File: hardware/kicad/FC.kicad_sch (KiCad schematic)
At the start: 6 parts, among them J6 xt30, U9 TPS7A4533DCQR

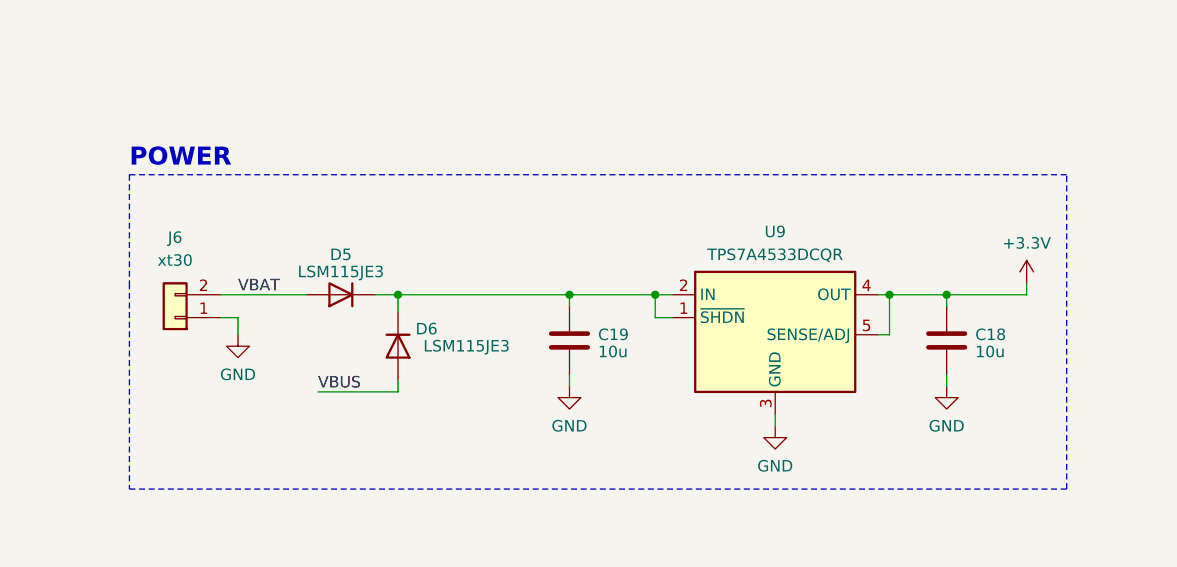
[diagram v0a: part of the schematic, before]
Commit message: assigned footprints
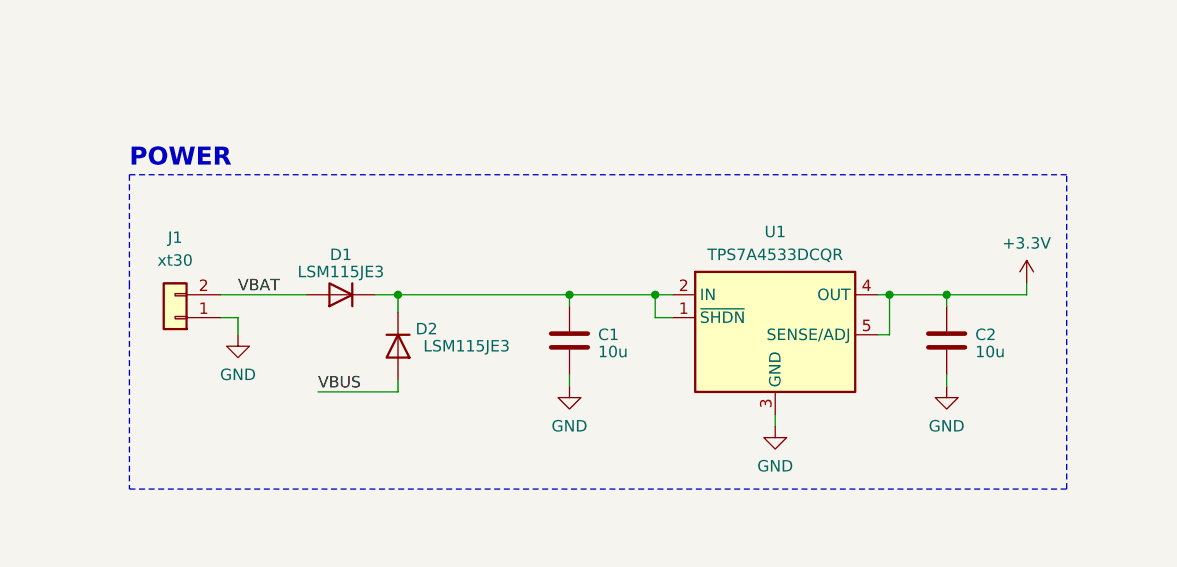
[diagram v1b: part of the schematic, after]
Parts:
- C1: renamed from C19; footprint (none) -> Resistor_SMD:R_0603_1608Metric
- C2: renamed from C18; footprint (none) -> Resistor_SMD:R_0603_1608Metric
- renumbered D5 to D1, D6 to D2, J6 to J1, U9 to U1
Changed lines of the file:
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@@
   (symbol (lib_id "Device:C") (at 208.915 152.4 0) (unit 1)
     (in_bom yes) (on_board yes) (dnp no)
-    (property "Reference" "C19" (at 212.09 151.765 0)
+    (property "Reference" "C1" (at 212.09 151.765 0)
       (effects (font (size 1.27 1.27)) (justify left))
     )
@@
       (effects (font (size 1.27 1.27)) (justify left))
     )
-    (property "Footprint" "" (at 209.8802 156.21 0)
+    (property "Footprint" "Resistor_SMD:R_0603_1608Metric" (at 209.8802 156.21 0)
       (effects (font (size 1.27 1.27)) hide)
     )
@@
       (project "FC"
         (path "/54cce219-8b98-4e71-96c4-f9ee784aa3bc"
-          (reference "C19") (unit 1)
+          (reference "C1") (unit 1)
         )
       )
@@
   (symbol (lib_id "Regulator_Linear:TPS7A05285PDBV") (at 231.775 149.86 0) (unit 1)
     (in_bom yes) (on_board yes) (dnp no) (fields_autoplaced)
-    (property "Reference" "U9" (at 231.775 140.335 0)
+    (property "Reference" "U1" (at 231.775 140.335 0)
       (effects (font (size 1.27 1.27)))
     )
@@
       (project "FC"
         (path "/54cce219-8b98-4e71-96c4-f9ee784aa3bc"
-          (reference "U9") (unit 1)
+          (reference "U1") (unit 1)
         )
       )
@@
   (symbol (lib_id "power:GND") (at 172.085 151.765 0) (unit 1)
     (in_bom yes) (on_board yes) (dnp no) (fields_autoplaced)
-    (property "Reference" "#PWR047" (at 172.085 158.115 0)
+    (property "Reference" "#PWR01" (at 172.085 158.115 0)
       (effects (font (size 1.27 1.27)) hide)
     )
@@
       (project "FC"
         (path "/54cce219-8b98-4e71-96c4-f9ee784aa3bc"
-          (reference "#PWR047") (unit 1)
+          (reference "#PWR01") (unit 1)
         )
       )
@@
   (symbol (lib_id "power:+3.3V") (at 259.715 146.05 0) (unit 1)
     (in_bom yes) (on_board yes) (dnp no) (fields_autoplaced)
-    (property "Reference" "#PWR045" (at 259.715 149.86 0)
+    (property "Reference" "#PWR05" (at 259.715 149.86 0)
       (effects (font (size 1.27 1.27)) hide)
     )
@@
       (project "FC"
         (path "/54cce219-8b98-4e71-96c4-f9ee784aa3bc"
-          (reference "#PWR045") (unit 1)
+          (reference "#PWR05") (unit 1)
         )
       )
@@
   (symbol (lib_id "Connector_Generic:Conn_01x02") (at 165.1 149.86 180) (unit 1)
     (in_bom yes) (on_board yes) (dnp no) (fields_autoplaced)
-    (property "Reference" "J6" (at 165.1 140.97 0)
+    (property "Reference" "J1" (at 165.1 140.97 0)
       (effects (font (size 1.27 1.27)))
     )
@@
       (project "FC"
         (path "/54cce219-8b98-4e71-96c4-f9ee784aa3bc"
-          (reference "J6") (unit 1)
+          (reference "J1") (unit 1)
         )
       )
@@
   (symbol (lib_id "power:GND") (at 250.825 157.48 0) (unit 1)
     (in_bom yes) (on_board yes) (dnp no) (fields_autoplaced)
-    (property "Reference" "#PWR043" (at 250.825 163.83 0)
+    (property "Reference" "#PWR04" (at 250.825 163.83 0)
       (effects (font (size 1.27 1.27)) hide)
     )
@@
       (project "FC"
         (path "/54cce219-8b98-4e71-96c4-f9ee784aa3bc"
-          (reference "#PWR043") (unit 1)
+          (reference "#PWR04") (unit 1)
         )
       )
@@
   (symbol (lib_id "Device:D") (at 183.515 147.32 180) (unit 1)
     (in_bom yes) (on_board yes) (dnp no)
-    (property "Reference" "D5" (at 183.515 142.875 0)
+    (property "Reference" "D1" (at 183.515 142.875 0)
       (effects (font (size 1.27 1.27)))
     )
@@
       (project "FC"
         (path "/54cce219-8b98-4e71-96c4-f9ee784aa3bc"
-          (reference "D5") (unit 1)
+          (reference "D1") (unit 1)
         )
       )
@@
   (symbol (lib_id "Device:C") (at 250.825 152.4 0) (unit 1)
     (in_bom yes) (on_board yes) (dnp no)
-    (property "Reference" "C18" (at 254 151.765 0)
+    (property "Reference" "C2" (at 254 151.765 0)
       (effects (font (size 1.27 1.27)) (justify left))
     )
@@
       (effects (font (size 1.27 1.27)) (justify left))
     )
-    (property "Footprint" "" (at 251.7902 156.21 0)
+    (property "Footprint" "Resistor_SMD:R_0603_1608Metric" (at 251.7902 156.21 0)
       (effects (font (size 1.27 1.27)) hide)
     )
@@
       (project "FC"
         (path "/54cce219-8b98-4e71-96c4-f9ee784aa3bc"
-          (reference "C18") (unit 1)
+          (reference "C2") (unit 1)
         )
       )
@@
   (symbol (lib_id "power:GND") (at 231.775 161.925 0) (unit 1)
     (in_bom yes) (on_board yes) (dnp no) (fields_autoplaced)
-    (property "Reference" "#PWR046" (at 231.775 168.275 0)
+    (property "Reference" "#PWR03" (at 231.775 168.275 0)
       (effects (font (size 1.27 1.27)) hide)
     )
@@
       (project "FC"
         (path "/54cce219-8b98-4e71-96c4-f9ee784aa3bc"
-          (reference "#PWR046") (unit 1)
+          (reference "#PWR03") (unit 1)
         )
       )
@@
   (symbol (lib_id "power:GND") (at 208.915 157.48 0) (unit 1)
     (in_bom yes) (on_board yes) (dnp no) (fields_autoplaced)
-    (property "Reference" "#PWR044" (at 208.915 163.83 0)
+    (property "Reference" "#PWR02" (at 208.915 163.83 0)
       (effects (font (size 1.27 1.27)) hide)
     )
@@
       (project "FC"
         (path "/54cce219-8b98-4e71-96c4-f9ee784aa3bc"
-          (reference "#PWR044") (unit 1)
+          (reference "#PWR02") (unit 1)
         )
       )
@@
   (symbol (lib_id "Device:D") (at 189.865 153.035 270) (unit 1)
     (in_bom yes) (on_board yes) (dnp no)
-    (property "Reference" "D6" (at 193.04 151.13 90)
+    (property "Reference" "D2" (at 193.04 151.13 90)
       (effects (font (size 1.27 1.27)))
     )
@@
       (project "FC"
         (path "/54cce219-8b98-4e71-96c4-f9ee784aa3bc"
-          (reference "D6") (unit 1)
-        )
-      )
+          (reference "D2") (unit 1)
+        )
+      )

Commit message: all footprints have been fixed
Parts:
- D1, D2: footprint (none) -> LSM115JE3:LSM115JE3
- J1: footprint (none) -> XT30PW-M:AMASS_XT30PW-M; Amazon (none) -> https://www.amazon.com/Amass-XT30PW-Upgrade-Connectors-Batt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
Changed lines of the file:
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@@
       (effects (font (size 1.27 1.27)))
     )
-    (property "Footprint" "" (at 165.1 149.86 0)
+    (property "Footprint" "XT30PW-M:AMASS_XT30PW-M" (at 162.56 139.7 0)
       (effects (font (size 1.27 1.27)) hide)
     )
     (property "Datasheet" "~" (at 165.1 149.86 0)
+      (effects (font (size 1.27 1.27)) hide)
+    )
+    (property "Amazon" "https://www.amazon.com/Amass-XT30PW-Upgrade-Connectors-Battery/dp/B099F2PXYN#customerReviews" (at 162.56 139.7 0)
       (effects (font (size 1.27 1.27)) hide)
     )
@@
       (effects (font (size 1.27 1.27)))
     )
-    (property "Footprint" "" (at 183.515 147.32 0)
+    (property "Footprint" "LSM115JE3:LSM115JE3" (at 183.515 147.32 0)
       (effects (font (size 1.27 1.27)) hide)
     )
@@
       (effects (font (size 1.27 1.27)))
     )
-    (property "Footprint" "" (at 189.865 153.035 0)
+    (property "Footprint" "LSM115JE3:LSM115JE3" (at 189.865 153.035 0)
       (effects (font (size 1.27 1.27)) hide)
     )

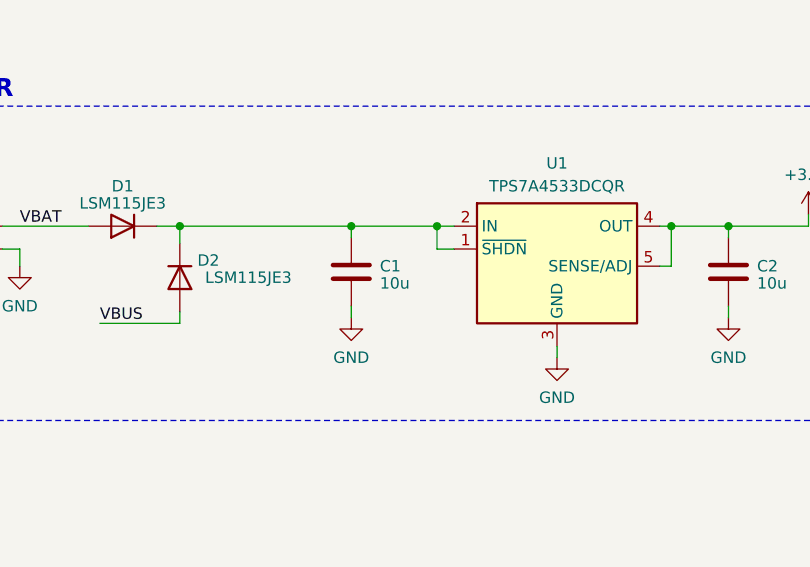
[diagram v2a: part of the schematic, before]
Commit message: changed cap footprint
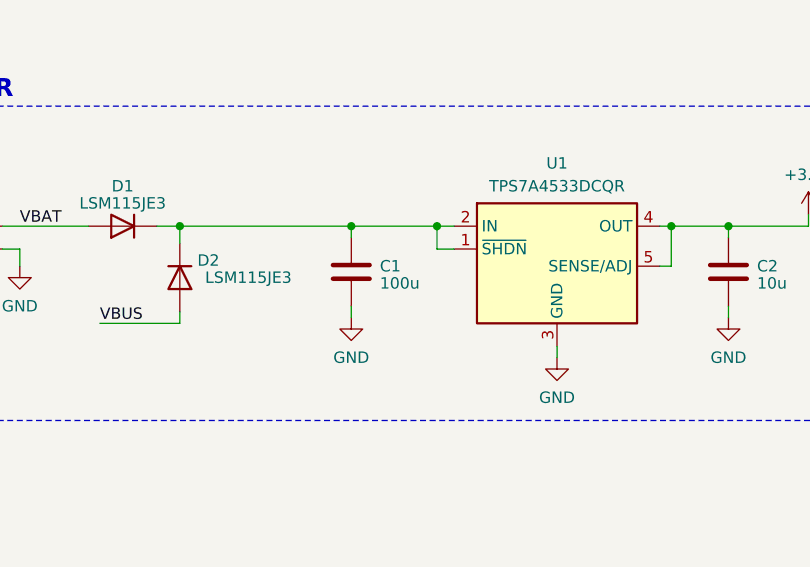
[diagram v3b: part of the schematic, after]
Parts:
- C1: value 10u -> 100u; footprint Resistor_SMD:R_0603_1608Metric -> Resistor_SMD:R_1206_3216Metric
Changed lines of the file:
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@@
       (effects (font (size 1.27 1.27)) (justify left))
     )
-    (property "Value" "10u" (at 212.09 153.67 0)
+    (property "Value" "100u" (at 212.09 153.67 0)
       (effects (font (size 1.27 1.27)) (justify left))
     )
-    (property "Footprint" "Resistor_SMD:R_0603_1608Metric" (at 209.8802 156.21 0)
+    (property "Footprint" "Resistor_SMD:R_1206_3216Metric" (at 209.8802 156.21 0)
       (effects (font (size 1.27 1.27)) hide)
     )

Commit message: ready for pcb
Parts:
- added D8: V15PM153, Package_TO_SOT_SMD:TO-277A, symbol Device:D_Schottky
- added F4: 30A, Resistor_SMD:R_1206_3216Metric, symbol Device:Fuse
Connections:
- net GND: now also D8.1 (A), D8.2 (A)
- net VBAT: now also D8.3 (K), F4.2; no longer J1.2 (N)
- new net: F4.1, J1.2 (N)
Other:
- moved on the sheet: J1
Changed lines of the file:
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@@
     (company "Missouri S&T Rocket Design Team")
   )
+  (junction (at 153.67 147.32) (diameter 0) (color 0 0 0 0)
+  )
   (junction (at 80.01 52.07) (diameter 0) (color 0 0 0 0)
+  )
+  (junction (at 153.67 156.21) (diameter 0) (color 0 0 0 0)
   )
   (junction (at 244.475 147.32) (diameter 0) (color 0 0 0 0)
@@
     (stroke (width 0) (type default))
   )
-  (wire (pts (xy 172.085 149.86) (xy 172.085 151.765))
-    (stroke (width 0) (type default))
-  )
   (wire (pts (xy 82.55 39.37) (xy 90.17 39.37))
     (stroke (width 0) (type default))
@@
     (stroke (width 0) (type default))
   )
+  (wire (pts (xy 134.62 147.32) (xy 142.24 147.32))
+    (stroke (width 0) (type default))
+  )
   (bus (pts (xy 154.94 52.07) (xy 192.405 52.07))
     (stroke (width 0) (type default))
@@
   )
   (wire (pts (xy 59.69 116.205) (xy 69.85 116.205))
+    (stroke (width 0) (type default))
+  )
+  (wire (pts (xy 136.525 156.21) (xy 153.67 156.21))
     (stroke (width 0) (type default))
   )
@@
     (stroke (width 0) (type default))
   )
-  (polyline (pts (xy 160.02 146.05) (xy 160.02 168.91))
-    (stroke (width 0) (type dash))
-  )
   (bus (pts (xy 15.24 180.34) (xy 15.24 184.15))
     (stroke (width 0) (type default))
   )
-  (wire (pts (xy 170.18 149.86) (xy 172.085 149.86))
+  (wire (pts (xy 153.67 156.21) (xy 153.67 158.115))
     (stroke (width 0) (type default))
   )
@@
     (stroke (width 0) (type dash))
   )
+  (wire (pts (xy 153.67 155.575) (xy 153.67 156.21))
+    (stroke (width 0) (type default))
+  )
   (wire (pts (xy 187.325 147.32) (xy 189.865 147.32))
     (stroke (width 0) (type default))
@@
     (stroke (width 0) (type dash))
   )
+  (wire (pts (xy 153.67 147.32) (xy 179.705 147.32))
+    (stroke (width 0) (type default))
+  )
   (bus (pts (xy 69.85 41.91) (xy 69.85 45.085))
     (stroke (width 0) (type default))
@@
   )
   (bus (pts (xy 229.87 41.91) (xy 229.87 45.085))
+    (stroke (width 0) (type default))
+  )
+  (wire (pts (xy 134.62 149.86) (xy 136.525 149.86))
     (stroke (width 0) (type default))
   )
@@
     (stroke (width 0) (type default))
   )
-  (polyline (pts (xy 160.02 133.985) (xy 160.02 146.05))
-    (stroke (width 0) (type dash))
-  )
   (wire (pts (xy 17.78 170.18) (xy 31.115 170.18))
     (stroke (width 0) (type default))
@@
     (stroke (width 0) (type default))
   )
+  (wire (pts (xy 153.67 147.32) (xy 153.67 147.955))
+    (stroke (width 0) (type default))
+  )
   (wire (pts (xy 59.69 123.825) (xy 69.85 123.825))
     (stroke (width 0) (type default))
@@
     (stroke (width 0) (type default))
   )
-  (wire (pts (xy 170.18 147.32) (xy 179.705 147.32))
+  (wire (pts (xy 149.86 147.32) (xy 153.67 147.32))
+    (stroke (width 0) (type default))
+  )
+  (wire (pts (xy 136.525 149.86) (xy 136.525 156.21))
     (stroke (width 0) (type default))
   )
@@
     )
   )
-  (symbol (lib_id "power:GND") (at 172.085 151.765 0) (unit 1)
+  (symbol (lib_id "power:GND") (at 153.67 158.115 0) (unit 1)
     (in_bom yes) (on_board yes) (dnp no) (fields_autoplaced)
-    (property "Reference" "#PWR01" (at 172.085 158.115 0)
-      (effects (font (size 1.27 1.27)) hide)
-    )
-    (property "Value" "GND" (at 172.085 156.21 0)
-      (effects (font (size 1.27 1.27)))
-    )
-    (property "Footprint" "" (at 172.085 151.765 0)
-      (effects (font (size 1.27 1.27)) hide)
-    )
-    (property "Datasheet" "" (at 172.085 151.765 0)
+    (property "Reference" "#PWR01" (at 153.67 164.465 0)
+      (effects (font (size 1.27 1.27)) hide)
+    )
+    (property "Value" "GND" (at 153.67 162.56 0)
+      (effects (font (size 1.27 1.27)))
+    )
+    (property "Footprint" "" (at 153.67 158.115 0)
+      (effects (font (size 1.27 1.27)) hide)
+    )
+    (property "Datasheet" "" (at 153.67 158.115 0)
       (effects (font (size 1.27 1.27)) hide)
     )
@@
     )
   )
-  (symbol (lib_id "Connector_Generic:Conn_01x02") (at 165.1 149.86 180) (unit 1)
+  (symbol (lib_id "Connector_Generic:Conn_01x02") (at 129.54 149.86 180) (unit 1)
     (in_bom yes) (on_board yes) (dnp no) (fields_autoplaced)
-    (property "Reference" "J1" (at 165.1 140.97 0)
-      (effects (font (size 1.27 1.27)))
-    )
-    (property "Value" "xt30" (at 165.1 143.51 0)
-      (effects (font (size 1.27 1.27)))
-    )
-    (property "Footprint" "XT30PW-M:AMASS_XT30PW-M" (at 162.56 139.7 0)
-      (effects (font (size 1.27 1.27)) hide)
-    )
-    (property "Datasheet" "~" (at 165.1 149.86 0)
-      (effects (font (size 1.27 1.27)) hide)
-    )
-    (property "Amazon" "https://www.amazon.com/Amass-XT30PW-Upgrade-Connectors-Battery/dp/B099F2PXYN#customerReviews" (at 162.56 139.7 0)
+    (property "Reference" "J1" (at 129.54 140.97 0)
+      (effects (font (size 1.27 1.27)))
+    )
+    (property "Value" "xt30" (at 129.54 143.51 0)
+      (effects (font (size 1.27 1.27)))
+    )
+    (property "Footprint" "XT30PW-M:AMASS_XT30PW-M" (at 127 139.7 0)
+      (effects (font (size 1.27 1.27)) hide)
+    )
+    (property "Datasheet" "~" (at 129.54 149.86 0)
+      (effects (font (size 1.27 1.27)) hide)
+    )
+    (property "Amazon" "https://www.amazon.com/Amass-XT30PW-Upgrade-Connectors-Battery/dp/B099F2PXYN#customerReviews" (at 127 139.7 0)
       (effects (font (size 1.27 1.27)) hide)
     )
@@
     )
   )
+  (symbol (lib_id "Device:D_Schottky") (at 153.67 151.765 270) (unit 1)
+    (in_bom yes) (on_board yes) (dnp no) (fields_autoplaced)
+    (property "Reference" "D8" (at 156.21 150.8125 90)
+      (effects (font (size 1.27 1.27)) (justify left))
+    )
+    (property "Value" "V15PM153" (at 156.21 153.3525 90)
+      (effects (font (size 1.27 1.27)) (justify left))
+    )
+    (property "Footprint" "Package_TO_SOT_SMD:TO-277A" (at 163.83 154.305 0)
+      (effects (font (size 1.27 1.27)) hide)
+    )
+    (property "Datasheet" "https://www.vishay.com/docs/87206/v15pm153.pdf" (at 163.83 154.305 0)
+      (effects (font (size 1.27 1.27)) hide)
+    )
+    (property "Digikey" "https://www.digikey.com/en/products/detail/vishay-general-semiconductor-diodes-division/V15PM153-M3-I/16683129" (at 163.83 154.305 0)
+      (effects (font (size 1.27 1.27)) hide)
+    )
+    (pin "3")
+    (pin "2")
+    (pin "1")
+    (instances
+      (project "FC"
+        (path "/54cce219-8b98-4e71-96c4-f9ee784aa3bc"
+          (reference "D8") (unit 1)
+        )
+      )
+    )
+  )
   (symbol (lib_id "Device:D") (at 183.515 147.32 180) (unit 1)
     (in_bom yes) (on_board yes) (dnp no)
@@
         )
       )
+    )
+  )
+  (symbol (lib_id "Device:Fuse") (at 146.05 147.32 90) (unit 1)
+    (in_bom yes) (on_board yes) (dnp no)
+    (property "Reference" "F4" (at 146.05 143.51 90)
+      (effects (font (size 1.27 1.27)))
+    )
+    (property "Value" "30A" (at 146.05 145.415 90)
+      (effects (font (size 1.27 1.27)))
+    )
+    (property "Footprint" "Resistor_SMD:R_1206_3216Metric" (at 146.05 149.098 90)
+      (effects (font (size 1.27 1.27)) hide)
+    )
+    (property "Datasheet" "https://www.belfuse.com/resources/datasheets/circuitprotection/ds-cp-c1h-series.pdf" (at 146.05 147.32 0)
+      (effects (font (size 1.27 1.27)) hide)
+    )
+    (property "Digikey" "https://www.digikey.com/en/products/detail/bel-fuse-inc/0685H9300-01/5466710?s=N4IgTCBcDaIAwDYAcBWAEgTgMxziAugL5A" (at 146.05 147.32 0)
+      (effects (font (size 1.27 1.27)) hide)
+    )
+    (pin "1")
+    (pin "2")
+    (instances
+      (project "FC"
+        (path "/54cce219-8b98-4e71-96c4-f9ee784aa3bc/047c0ef5-e762-41a7-bfd7-fdc982a27304"
+          (reference "F4") (unit 1)
+        )
+        (path "/54cce219-8b98-4e71-96c4-f9ee784aa3bc"
+          (reference "F2") (unit 1)
+        )
+      )

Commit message: sync
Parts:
- J1: footprint XT30PW-M:AMASS_XT30PW-M -> Connector_AMASS:AMASS_XT30PW-M_1x02_P2.50mm_Horizontal
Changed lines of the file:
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@@
       (effects (font (size 1.27 1.27)))
     )
-    (property "Footprint" "XT30PW-M:AMASS_XT30PW-M" (at 127 139.7 0)
+    (property "Footprint" "Connector_AMASS:AMASS_XT30PW-M_1x02_P2.50mm_Horizontal" (at 127 139.7 0)
       (effects (font (size 1.27 1.27)) hide)
     )
